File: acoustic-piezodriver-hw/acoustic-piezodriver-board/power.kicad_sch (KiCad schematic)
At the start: 0 parts

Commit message: [piezodriver] Added piezo-driver board connectors
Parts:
- added J2: Conn_02x04_Odd_Even, Connector_PinHeader_2.54mm:PinHeader_2x04_P2.54mm_Horizontal, symbol Connector_Generic:Conn_02x04_Odd_Even
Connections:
- new net +5V: J2.1 (Pin_1), J2.3 (Pin_3), J2.5 (Pin_5), J2.7 (Pin_7)
- new net GND: J2.2 (Pin_2), J2.4 (Pin_4), J2.6 (Pin_6), J2.8 (Pin_8)

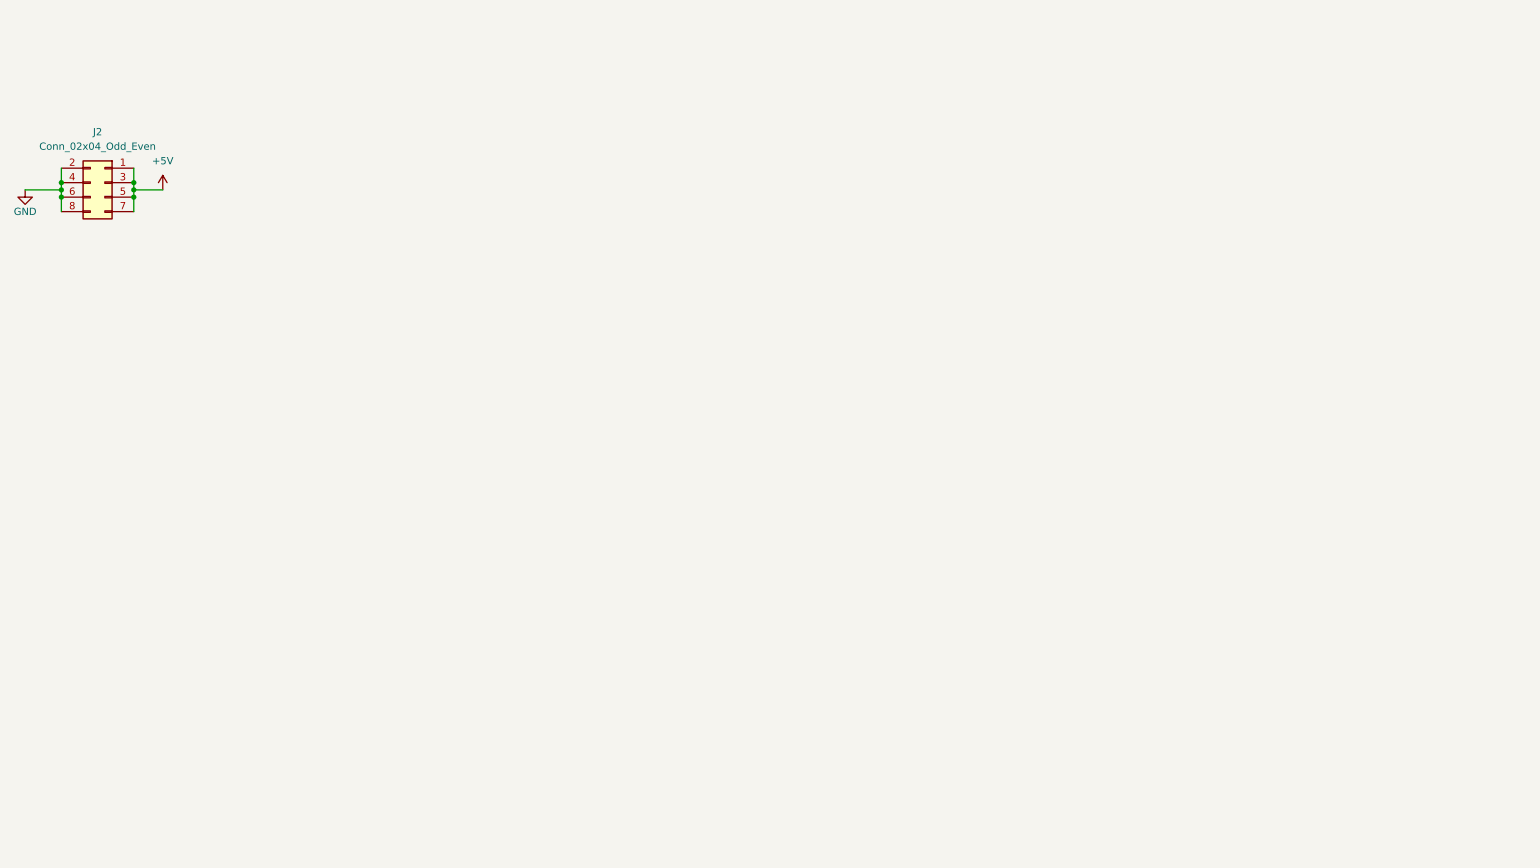
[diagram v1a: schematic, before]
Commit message: [piezodriver] Changed piezodriver hardware, (next) create simulations in ltspice, pick components
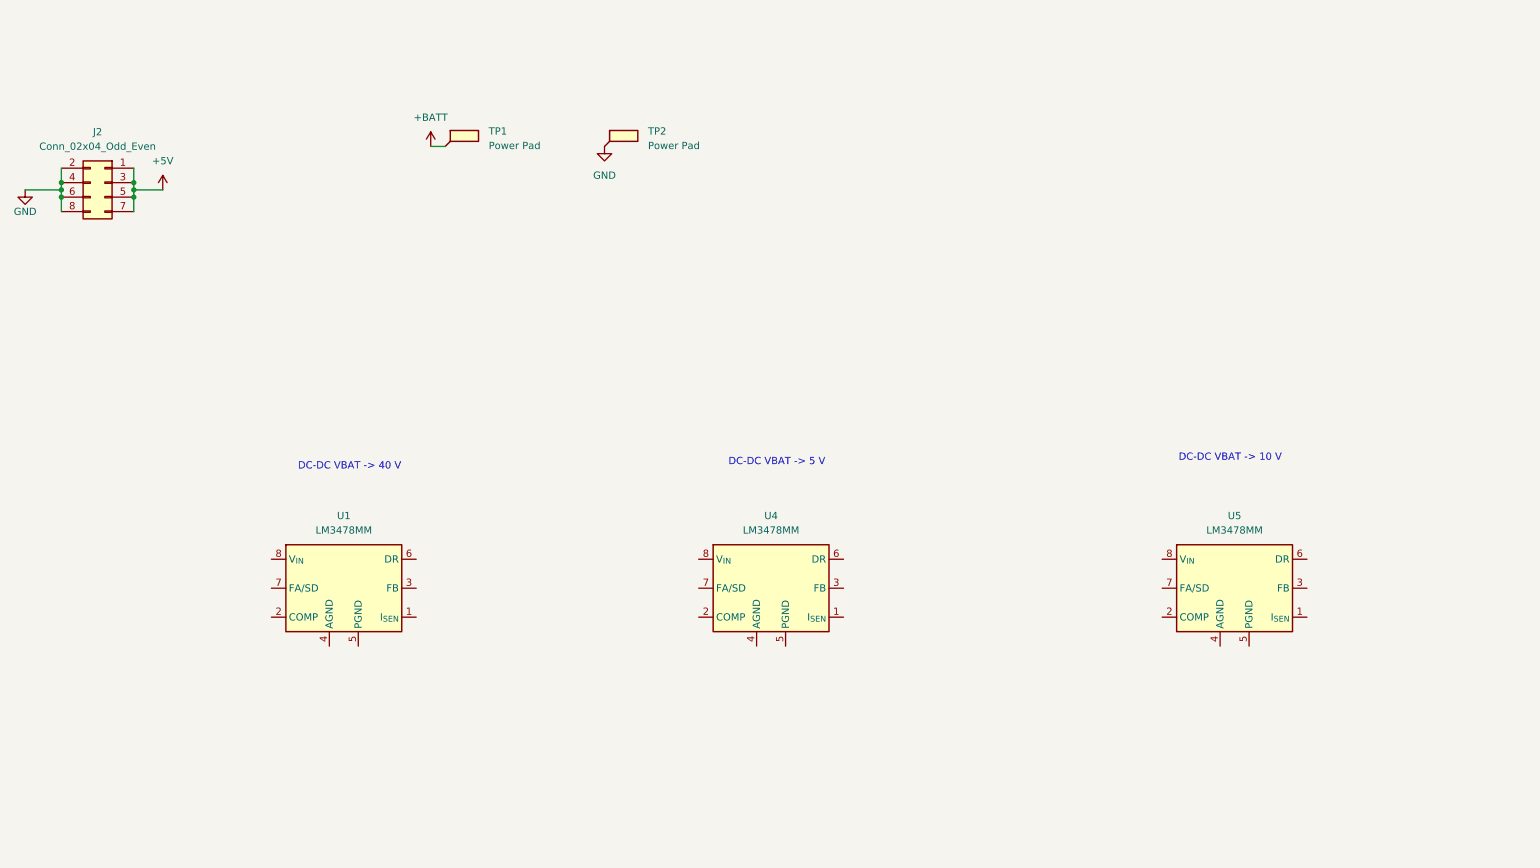
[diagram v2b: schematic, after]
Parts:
- added TP1, TP2: Power Pad, TestPoint:TestPoint_Pad_4.0x4.0mm, symbol Connector:TestPoint_Flag
- added U1, U4, U5: LM3478MM, Package_SO:VSSOP-8_3x3mm_P0.65mm, symbol Regulator_Controller:LM3478MM
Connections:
- net GND: now also TP2.1
- new net +BATT: TP1.1
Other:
- note added: "DC-DC VBAT -> 10 V"
- note added: "DC-DC VBAT -> 40 V"
- note added: "DC-DC VBAT -> 5 V"

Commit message: [driver] added components to sepic, added notes
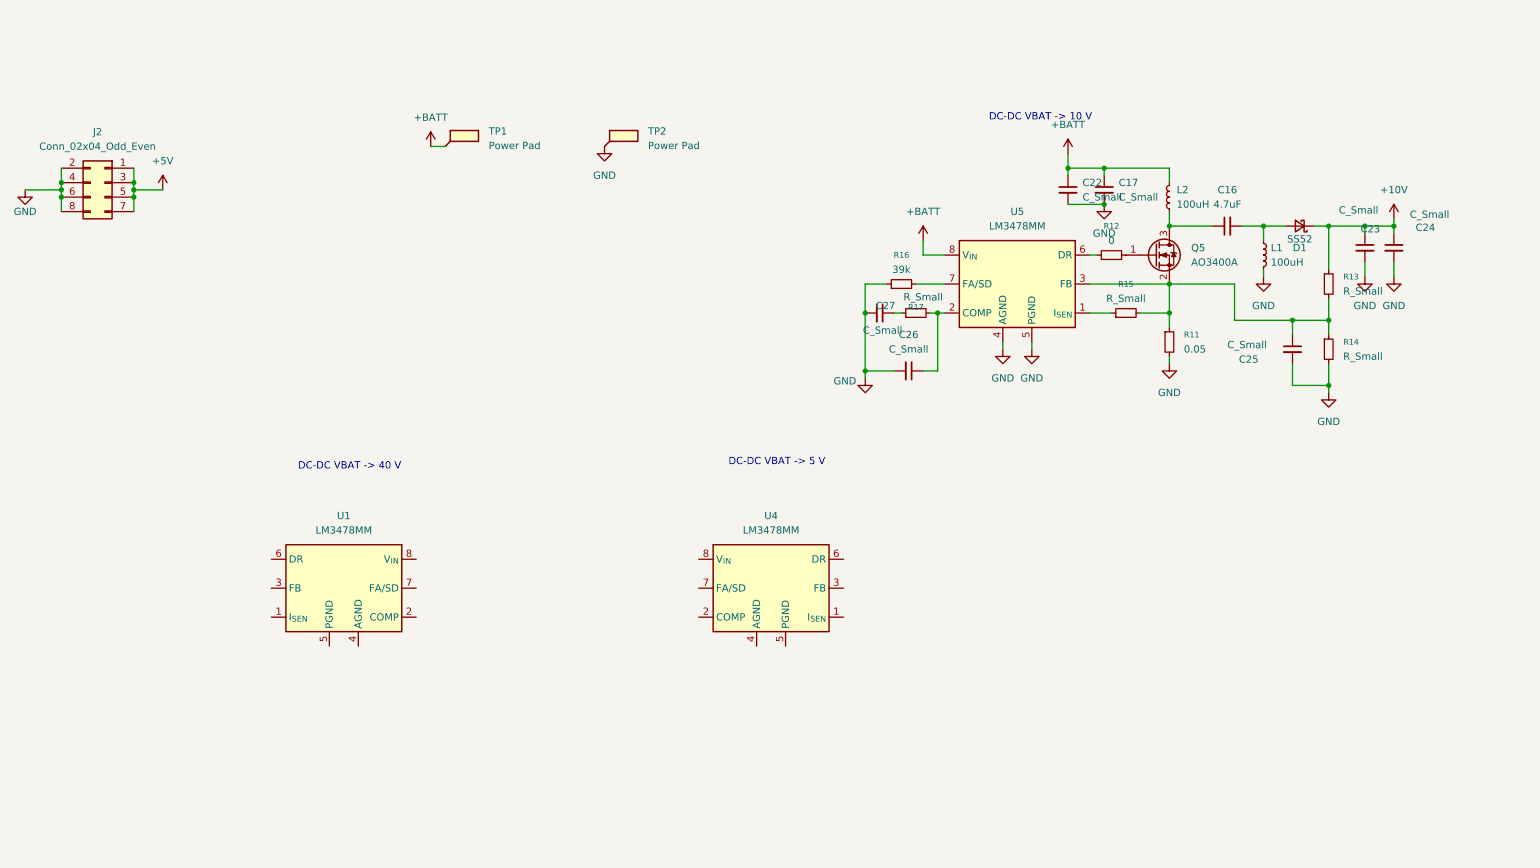
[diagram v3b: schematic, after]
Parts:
- added C16: 4.7uF, Capacitor_SMD:C_1206_3216Metric, symbol Device:C_Small
- added C17, C22, C23, C24, C25, C26, C27: C_Small, symbol Device:C_Small
- added D1: SS52, Diode_SMD:D_SMA-SMB_Universal_Handsoldering, symbol Device:D_Schottky_Small
- added L1, L2: 100uH, symbol Device:L_Small
- added Q5: AO3400A, Package_TO_SOT_SMD:SOT-23, symbol Transistor_FET:AO3400A
- added R11: 0.05, Resistor_SMD:R_1206_3216Metric_Pad1.30x1.75mm_HandSolder, symbol Device:R_Small
- added R12: 0, symbol Device:R_Small
- added R13, R14, R15, R17: R_Small, symbol Device:R_Small
- added R16: 39k, Resistor_SMD:R_0603_1608Metric, symbol Device:R_Small
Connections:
- net +BATT: now also U5.8 (V_{IN}), C17.1, C22.1, L2.2
- net GND: now also U5.4 (AGND), U5.5 (PGND), C17.2, C22.2, C23.2, C24.2, C25.2, C26.2, C27.2, L1.2, R11.2, R14.2, R16.1
- net at U5.1 (I_{SEN}): now also R15.1
- net at U5.2 (COMP): now also C26.1, R17.2
- net at U5.3 (FB): now also C25.1, Q5.2 (S), R11.1, R13.2, R14.1, R15.2
- net at U5.6 (DR): now also R12.1
- net at U5.7 (FA/SD): now also R16.2
- new net: C16.2, D1.2 (A), L1.1
- new net: C16.1, L2.1, Q5.3 (D)
- new net: Q5.1 (G), R12.2
- new net: C27.1, R17.1
- new net +10V: C23.1, C24.1, D1.1 (K), R13.1
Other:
- moved on the sheet: U5

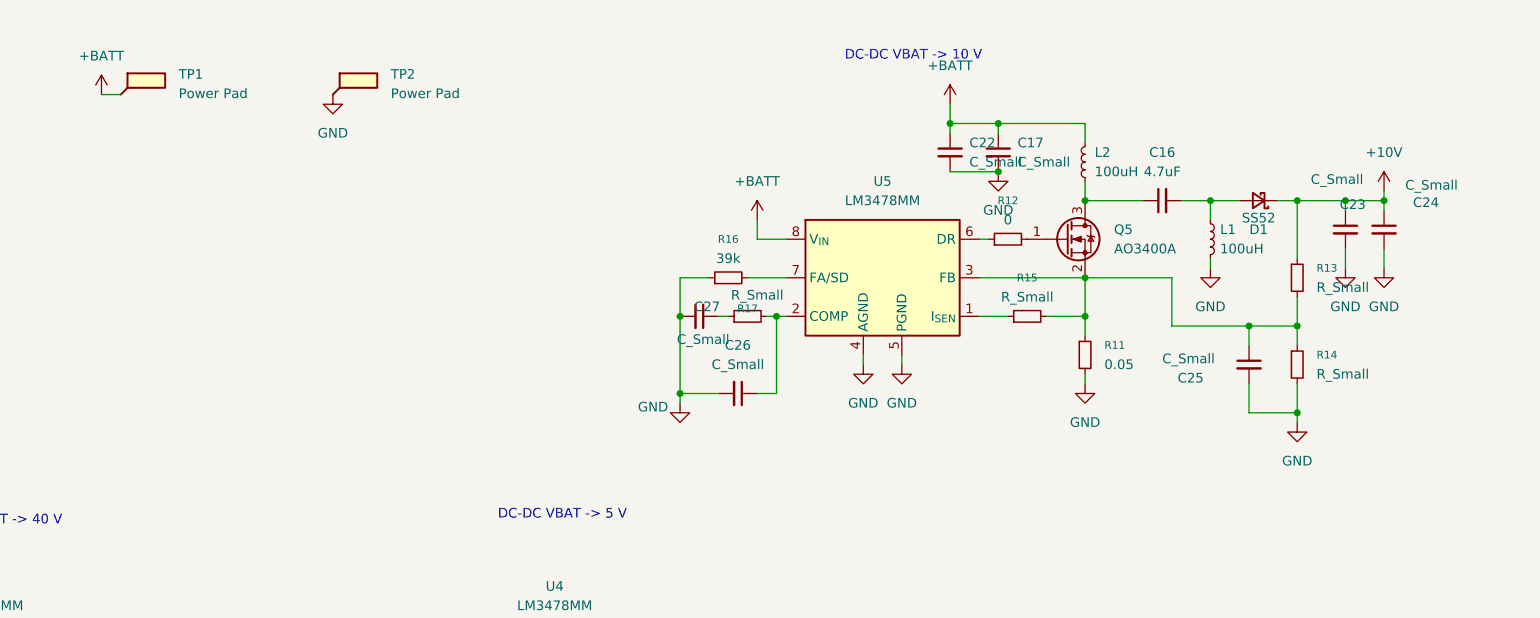
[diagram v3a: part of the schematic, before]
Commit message: [piezodriver] Added X7R input capacitor, add input and output capacitance of 40-100 uF
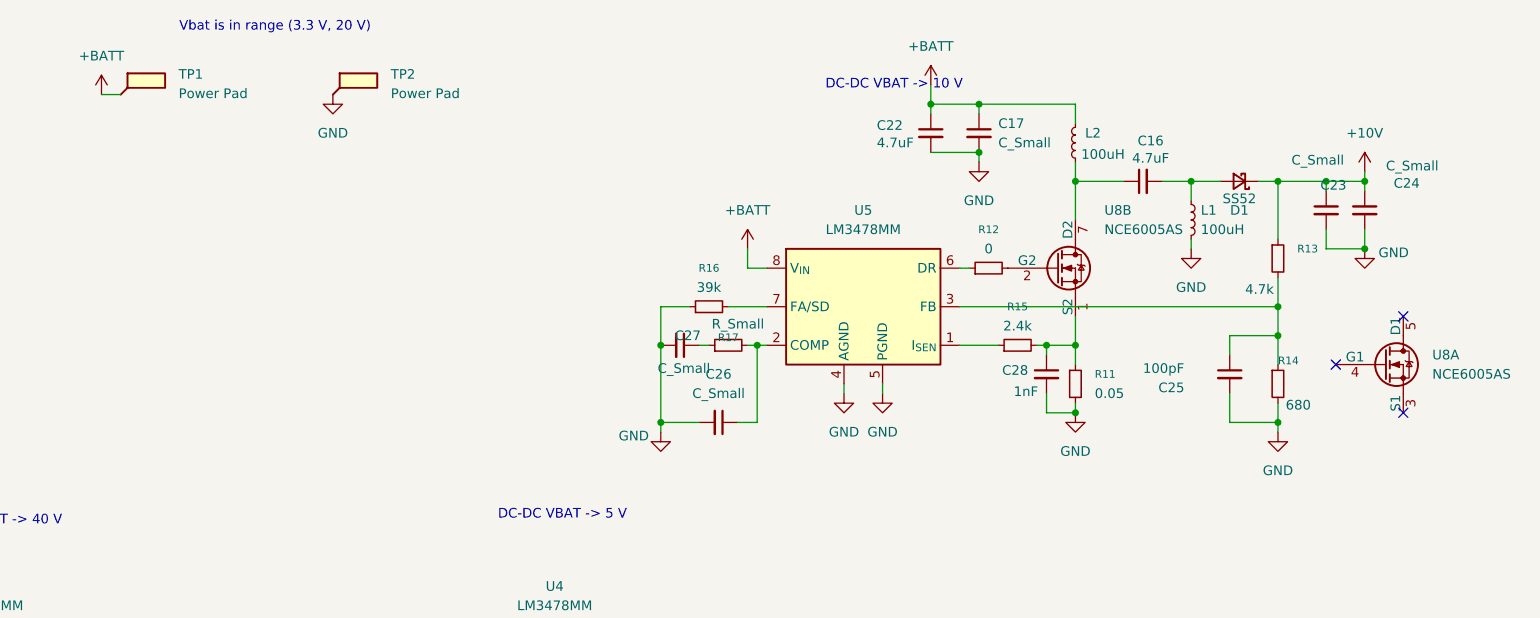
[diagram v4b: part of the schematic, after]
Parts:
- removed Q5: AO3400A, Package_TO_SOT_SMD:SOT-23, symbol Transistor_FET:AO3400A
- added C28: 1nF, symbol Device:C_Small
- added U8: NCE6005AS, symbol custom_mosfet:NCE6005AS
- C22: value C_Small -> 4.7uF; footprint (none) -> Capacitor_SMD:C_1206_3216Metric; LPN (none) -> C29823; MPN (none) -> 1206B475K500NT
- C25: value C_Small -> 100pF
- R13: value R_Small -> 4.7k; footprint (none) -> Resistor_SMD:R_0603_1608Metric; LPN (none) -> C23162; MPN (none) -> 0603WAF4701T5E
- R14: value R_Small -> 680; footprint (none) -> Resistor_SMD:R_0603_1608Metric; LPN (none) -> C23228; MPN (none) -> 0603WAF6800T5E
- R15: value R_Small -> 2.4k; footprint (none) -> Resistor_SMD:R_0805_2012Metric_Pad1.20x1.40mm_HandSolder; LPN (none) -> C17526; MPN (none) -> 0805W8F2401T5E
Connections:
- net GND: now also C28.2
- net at C25.1, R13.2, R14.1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: no longer R11.1, R15.2
- net at C16.1, L2.1: now also U8.7 (D2), U8.8 (D2)
- net at R12.2: now also U8.2 (G2)
- new net: C28.1, R11.1, R15.2, U8.1 (S2)
- new net: U8.5 (D1), U8.6 (D1)
- no-connect marks 0 -> 3
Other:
- note added: "Vbat is in range (3.3 V, 20 V)"
- moved on the sheet: C16, C17, C22, C23, C24, C25, C26, C27, D1, L1, L2, R11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

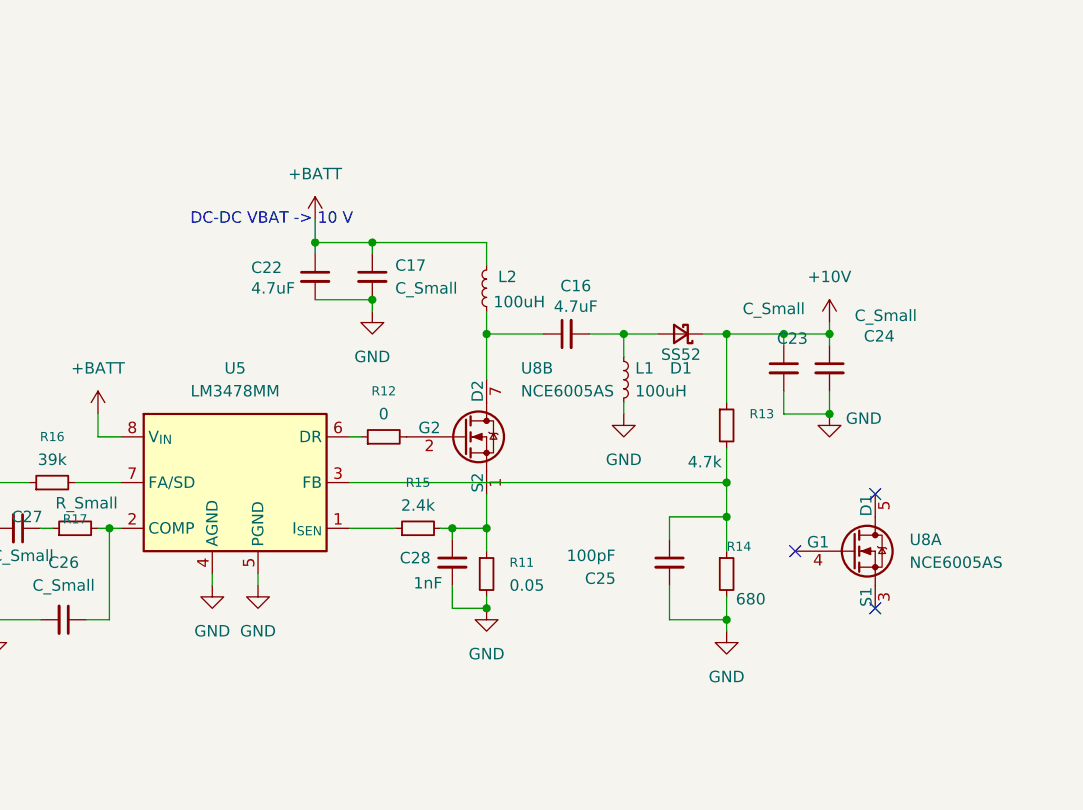
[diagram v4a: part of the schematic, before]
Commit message: [piezodriver] Added input and output capacitor to 10 V sepic
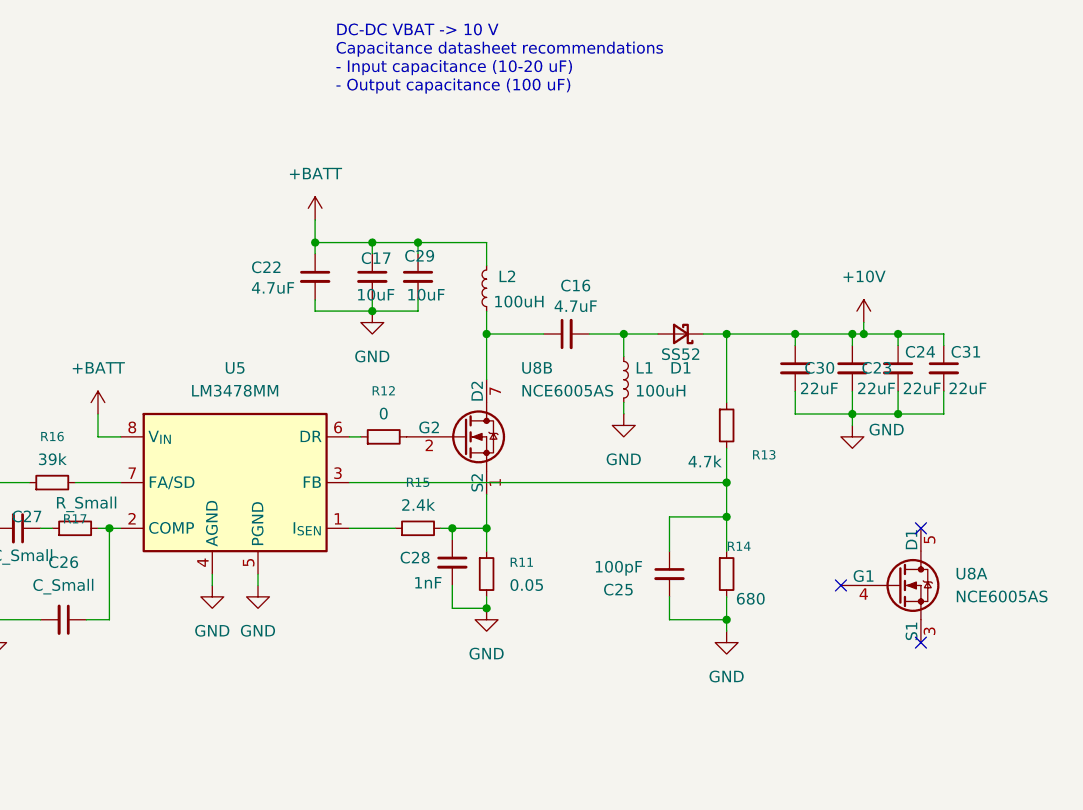
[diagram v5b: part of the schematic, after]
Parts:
- added C29: 10uF, Capacitor_SMD:C_0805_2012Metric, symbol Device:C_Small
- added C30, C31: 22uF, Capacitor_SMD:C_0805_2012Metric, symbol Device:C_Small
- C17: value C_Small -> 10uF; footprint (none) -> Capacitor_SMD:C_0805_2012Metric; LPN (none) -> C440198; MPN (none) -> GRM21BR61H106KE43L
- C23, C24: value C_Small -> 22uF; footprint (none) -> Capacitor_SMD:C_0805_2012Metric; LPN (none) -> C45783; MPN (none) -> CL21A226MAQNNNE
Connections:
- net +10V: now also C30.1, C31.1
- net +BATT: now also C29.1
- net GND: now also C29.2, C30.2, C31.2
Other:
- note added: "DC-DC VBAT -> 10 V Capacitance datasheet recommendations - Input capacitance (10-20 uF) - Output capacitance (100 uF)"
- note removed: "DC-DC VBAT -> 10 V"
- moved on the sheet: C23, C25, U8A
